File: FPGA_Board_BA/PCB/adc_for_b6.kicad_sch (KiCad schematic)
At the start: 6 parts, among them J201 PinHeader_03_male, U201 LTC2320-16_LVDS

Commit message: work
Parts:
- removed U201: LTC2320-16_LVDS, MYLIB_chips:UKG_52_7mm_8mm, symbol MYLIB_U:LTC2320-16_LVDS
- added C1, C11, C2: 1u_0603, WLIB_Capacitor:C_0603, symbol WLIB_C:1u_0603
- added C10, C3, C4, C5, C6, C7, C8, C9: 100n_0603, WLIB_Capacitor:C_0603, symbol WLIB_C:100n_0603
- added Q1: NTR5103NT1G, Package_TO_SOT_SMD:SOT-23_Handsoldering, symbol WLIB_Q:NTR5103NT1G
- added R5: 100R_0603, Resistor_SMD:R_0603_1608Metric, symbol WLIB_R:100R_0603
- added R6, R7: 10k_0603, Resistor_SMD:R_0603_1608Metric, symbol WLIB_R:10k_0603
- added U1: LTC2320-16_CMOS, MYLIB_chips:UKG_52_7mm_8mm, symbol MYLIB_U:LTC2320-16_CMOS
- renumbered C202 to C12, C201 to C13, C203 to C14, C204 to C15, J201 to J1
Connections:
- net +1V8: now also C1.1, C10.1, C4.1, C6.1, C8.1, R7.1, U1.31 (OVDD), U1.37 (OVDD)
- net +5VA: now also C2.1, C3.1, C5.1, C7.1, C9.1, U1.15 (VDD), U1.21 (VDD), U1.43 (REFBUFEN), U1.44 (VDD), U1.52 (VDD)
- net CLK_IN: now also U1.41 (SCK)
- net CLK_OUT: now also U1.33 (CLKOUT+)
- net Diffamp1/Ain+: now also U1.20 (Ain1+)
- net Diffamp1/Ain-: now also U1.19 (Ain1-)
- net Diffamp2/Ain+: now also U1.17 (Ain2+)
- net Diffamp2/Ain-: now also U1.16 (Ain2-)
- net Diffamp3/Ain+: now also U1.14 (Ain3+)
- net Diffamp3/Ain-: now also U1.13 (Ain3-)
- net Diffamp4/Ain+: now also U1.11 (Ain4+)
- net Diffamp4/Ain-: now also U1.10 (Ain4-)
- net Diffamp5/Ain+: now also U1.5 (Ain5+)
- net Diffamp5/Ain-: now also U1.4 (Ain5-)
- net Diffamp6/Ain+: now also U1.2 (Ain6+)
- net Diffamp6/Ain-: now also U1.1 (Ain6-)
- net Diffamp7/Ain+: now also U1.51 (Ain7+)
- net Diffamp7/Ain-: now also U1.50 (Ain7-)
- net Diffamp8/Ain+: now also U1.48 (Ain8+)
- net Diffamp8/Ain-: now also U1.47 (Ain8-)
- net GND: now also C1.2, C10.2, C11.2, C2.2, C3.2, C4.2, C5.2, C6.2, C7.2, C8.2, C9.2, Q1.2 (S), R6.2, U1.12 (GND), U1.18 (GND), U1.25 (~{CMOS}/LVDS), U1.26 (GND), U1.3 (GND), U1.32 (GND), U1.34 (CLKOUT-), U1.38 (GND), U1.46 (GND), U1.49 (GND), U1.53 (GND), U1.7 (GND)
- net SDO1: now also U1.27 (SDO1)
- net SDO2: now also U1.28 (SDO2)
- net SDO3: now also U1.29 (SDO3)
- net SDO4: now also U1.30 (SDO4)
- net SDO5: now also U1.35 (SDO5)
- net SDO6: now also U1.36 (SDO6)
- net SDO7: now also U1.39 (SDO7)
- net SDO8: now also U1.40 (SDO8)
- net ~{CNV}: now also Q1.3 (D), R7.2, U1.24 (~{CNV})
- net at C14.1: now also U1.6 (REFOUT3)
- net at C15.1: now also U1.45 (REFOUT4)
- net at C13.1: now also U1.9 (REFOUT2)
- net at C12.1: now also U1.22 (REFOUT1)
- net at J1.2 (Pin_2): now also U1.23 (~{SDR}/DDR)
- new net: C11.1, U1.8 (REF)
- new net: Q1.1 (G), R5.2, R6.1
- new net CNV: R5.1
- no-connect marks 2 -> 1

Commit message: 18.11 Bib Session
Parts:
- removed Q1: NTR5103NT1G, Package_TO_SOT_SMD:SOT-23_Handsoldering, symbol WLIB_Q:NTR5103NT1G
- removed R5: 100R_0603, Resistor_SMD:R_0603_1608Metric, symbol WLIB_R:100R_0603
- removed R6, R7: 10k_0603, Resistor_SMD:R_0603_1608Metric, symbol WLIB_R:10k_0603
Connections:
- net CLK_IN: no longer U1.41 (SCK)
- net ~{CNV}: no longer U1.24 (~{CNV})
- new net Level Shift for DIO/B1: U1.41 (SCK)
- new net Level Shift for DIO/B2: U1.24 (~{CNV})
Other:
- added sheet Level Shift for DIO (ls_for_dio.kicad_sch)

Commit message: exported stuff
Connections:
- net REFOUT_B6: now reaches C11.1, U1.8 (REF)
- net Diffamp1/Ain+ renamed Diffamp_1/Ain+
- net Diffamp1/Ain- renamed Diffamp_1/Ain-
- net Diffamp2/Ain+ renamed Diffamp_2/Ain+
- net Diffamp2/Ain- renamed Diffamp_2/Ain-
- net Diffamp3/Ain+ renamed Diffamp_3/Ain+
- net Diffamp3/Ain- renamed Diffamp_3/Ain-
- net Diffamp4/Ain+ renamed Diffamp_4/Ain+
- net Diffamp4/Ain- renamed Diffamp_4/Ain-
- net Diffamp5/Ain+ renamed Diffamp_5/Ain+
- net Diffamp5/Ain- renamed Diffamp_5/Ain-
- net Diffamp6/Ain+ renamed Diffamp_6/Ain+
- net Diffamp6/Ain- renamed Diffamp_6/Ain-
- net Diffamp7/Ain+ renamed Diffamp_7/Ain+
- net Diffamp7/Ain- renamed Diffamp_7/Ain-
- net Diffamp8/Ain+: no longer names the net of U1.48 (Ain8+)
- net Diffamp8/Ain-: no longer names the net of U1.47 (Ain8-)
- no-connect marks 1 -> 2
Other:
- removed sheet Diffamp1
- removed sheet Diffamp2
- removed sheet Diffamp3
- removed sheet Diffamp4
- removed sheet Diffamp5
- removed sheet Diffamp6
- removed sheet Diffamp7
- removed sheet Diffamp8
- added sheet Diffamp_1 (diffamp_.kicad_sch)
- added sheet Diffamp_2 (diffamp_.kicad_sch)
- added sheet Diffamp_3 (diffamp_.kicad_sch)
- added sheet Diffamp_4 (diffamp_.kicad_sch)
- added sheet Diffamp_5 (diffamp_.kicad_sch)
- added sheet Diffamp_6 (diffamp_.kicad_sch)
- added sheet Diffamp_7 (diffamp_.kicad_sch)

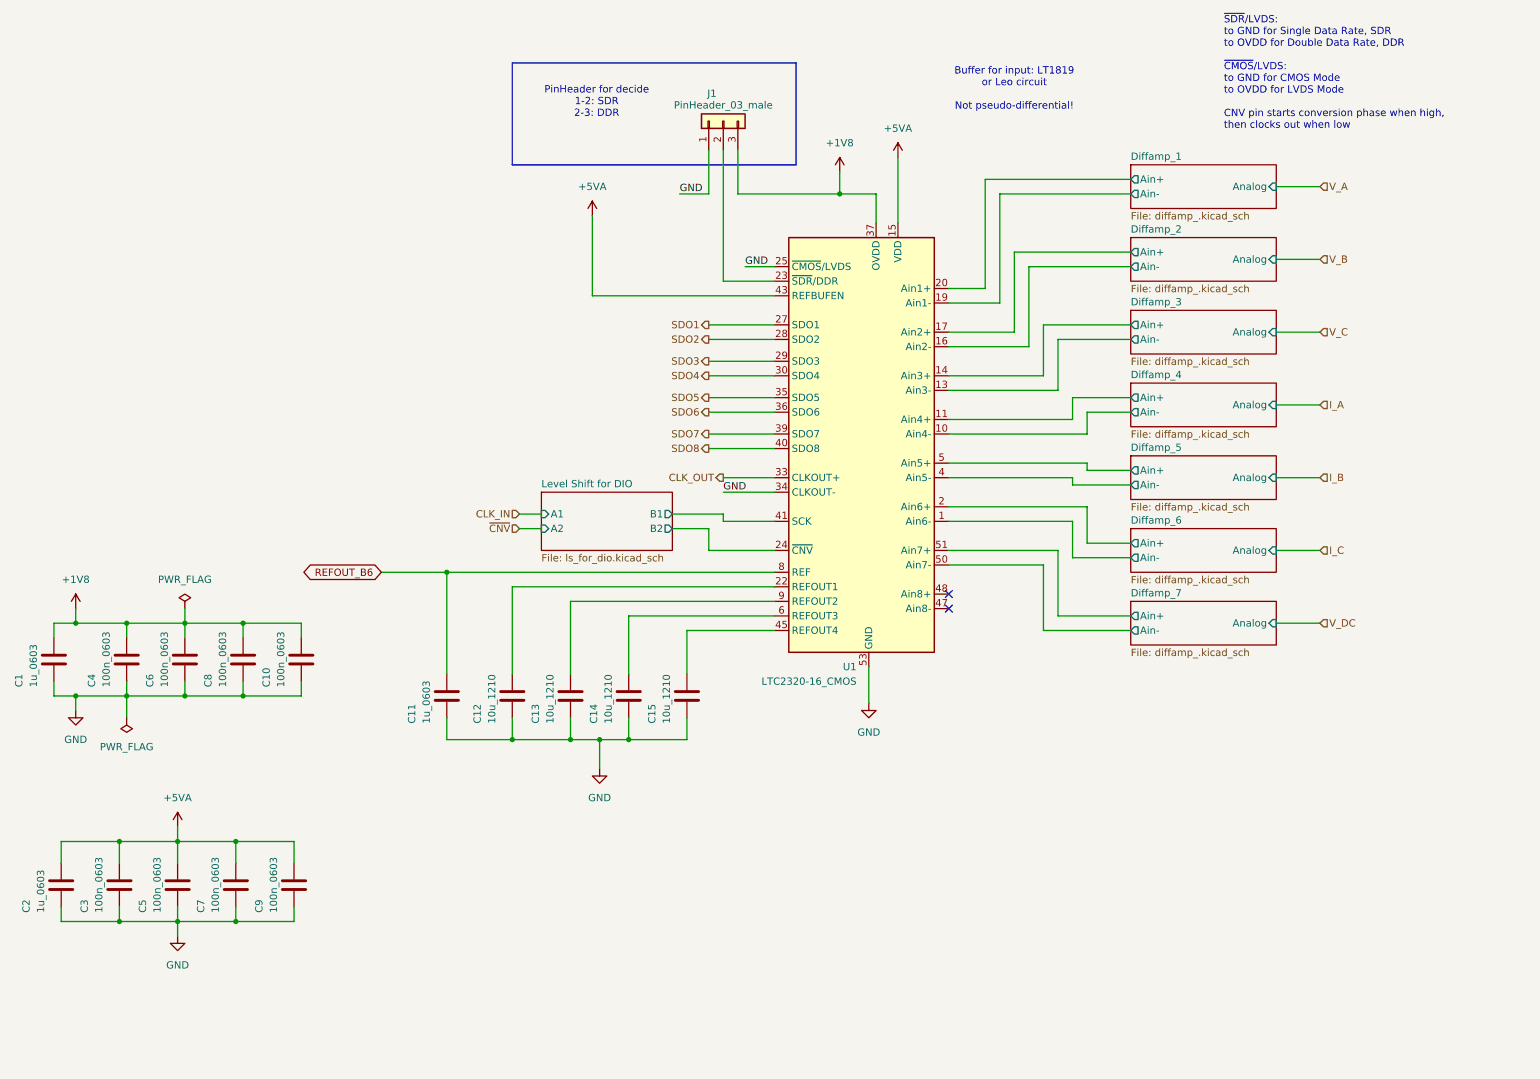
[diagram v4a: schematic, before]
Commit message: arranged level shifters in schematic + solid progress in layout
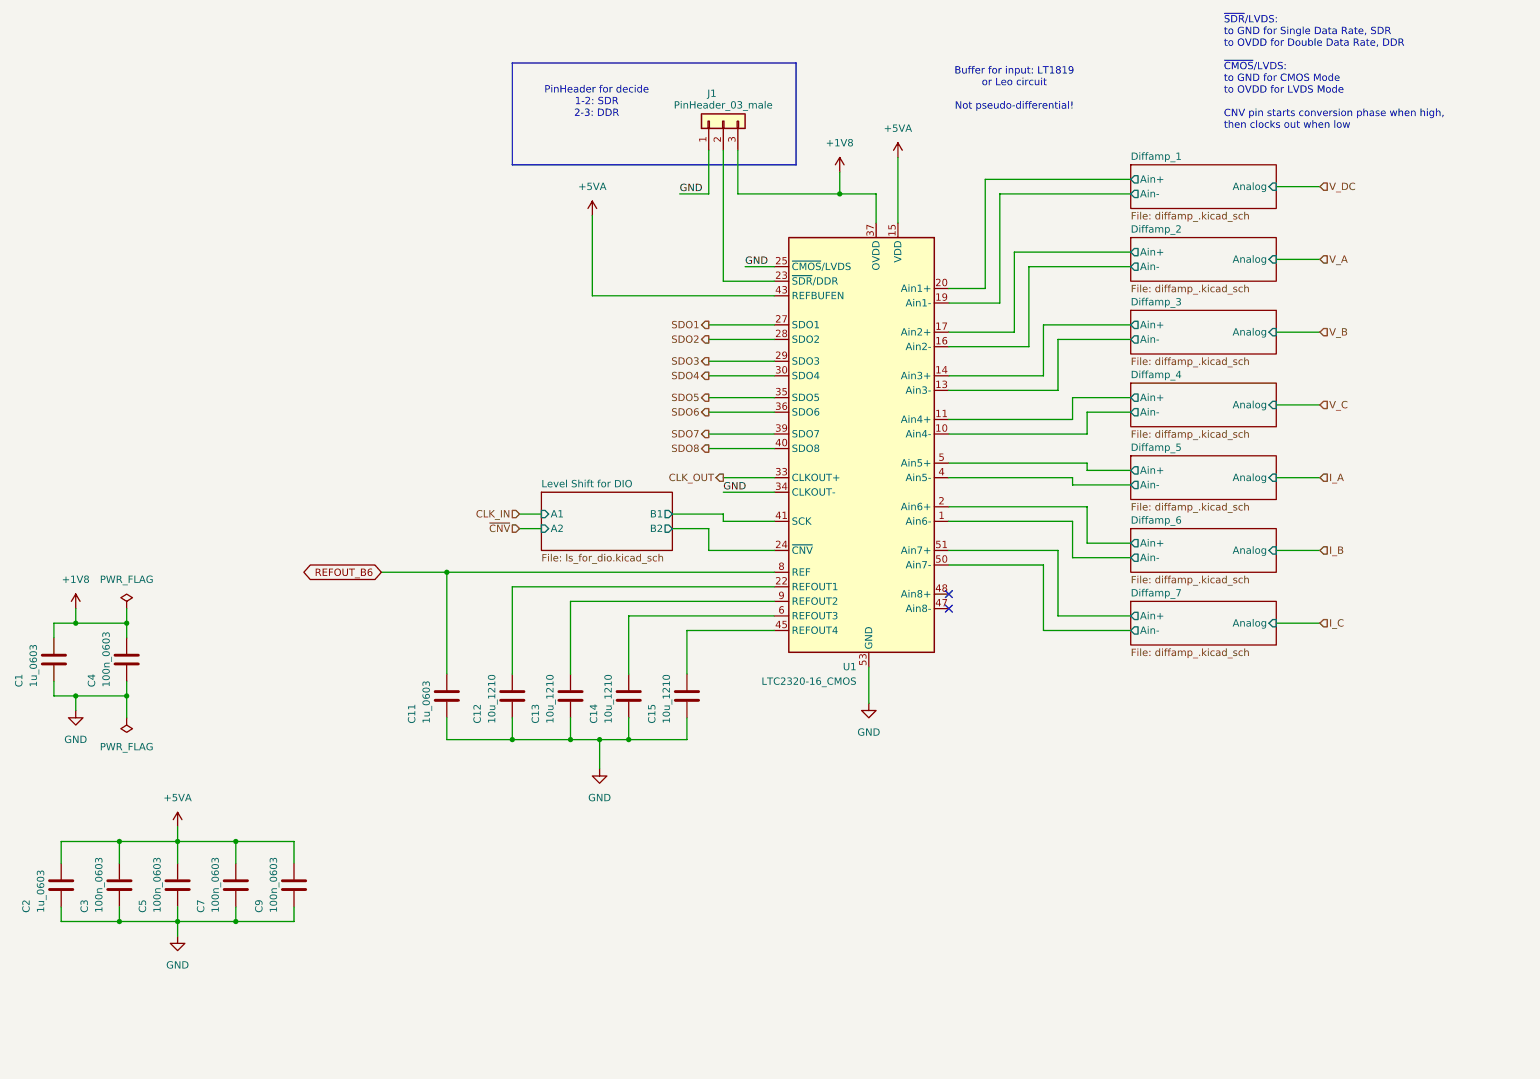
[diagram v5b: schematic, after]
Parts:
- removed C10, C6, C8: 100n_0603, WLIB_Capacitor:C_0603, symbol WLIB_C:100n_0603

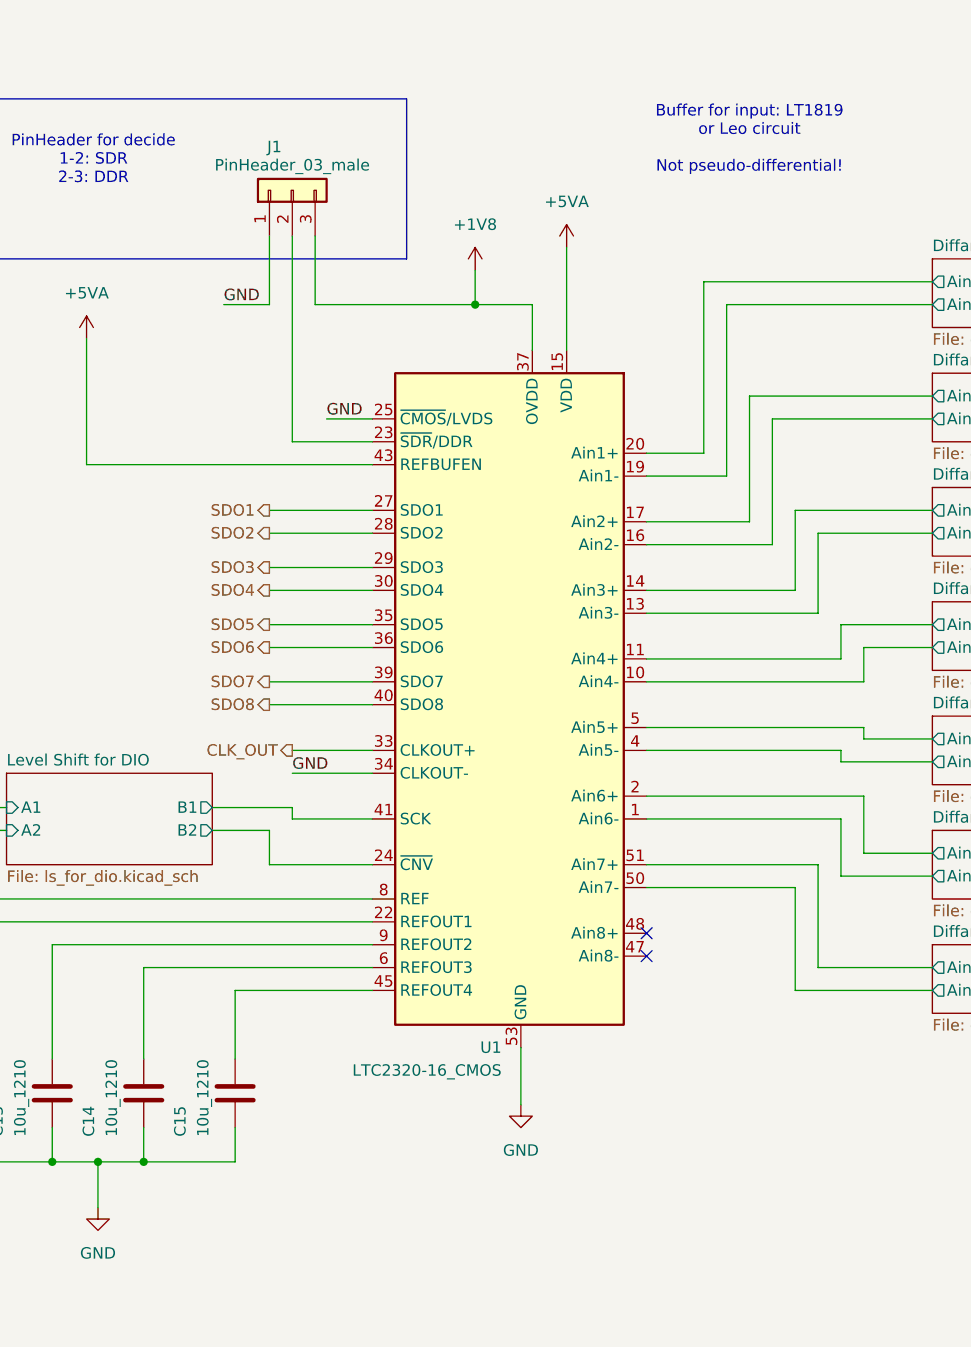
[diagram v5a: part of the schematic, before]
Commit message: component placement with new concept is ready
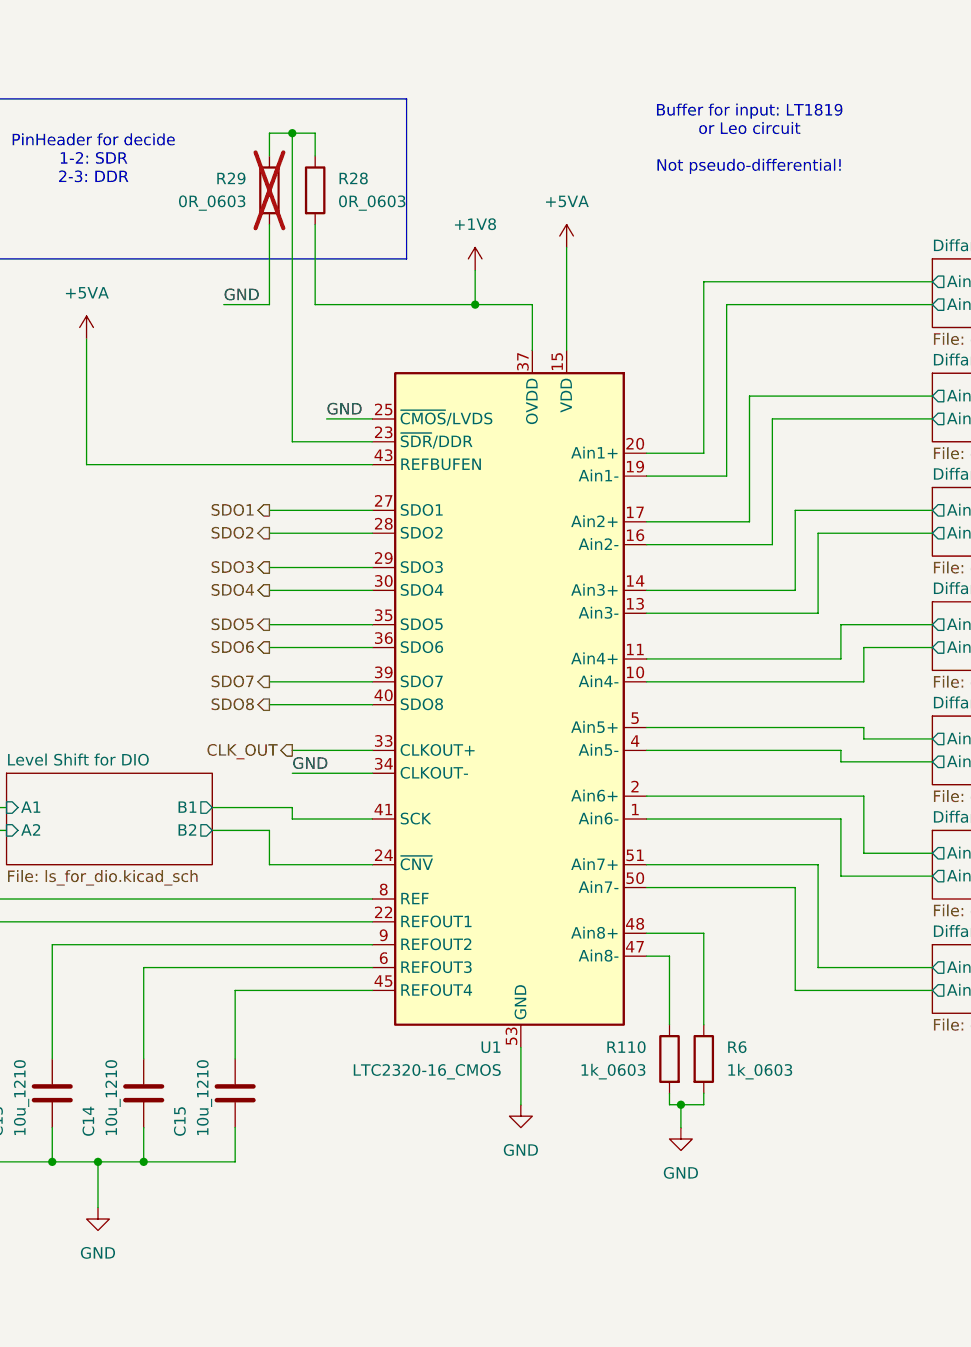
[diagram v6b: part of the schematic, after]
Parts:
- removed J1: PinHeader_03_male, Connector_PinHeader_2.54mm:PinHeader_1x03_P2.54mm_Vertical, symbol WLIB_J:PinHeader_03_male
- added R110, R6: 1k_0603, Resistor_SMD:R_0603_1608Metric, symbol WLIB_R:1k_0603
- added R28, R29: 0R_0603, Resistor_SMD:R_0603_1608Metric, symbol WLIB_R:0R_0603
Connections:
- net +1V8: now also R28.2
- net GND: now also R110.2, R29.2, R6.2
- net at U1.23 (~{SDR}/DDR): now also R28.1, R29.1
- net at U1.47 (Ain8-): now also R110.1
- net at U1.48 (Ain8+): now also R6.1
- no-connect marks 2 -> 0
